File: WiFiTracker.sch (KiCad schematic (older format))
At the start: 33 parts, among them IC1 CP2104, P1 ANT, P2 Battery, P3 USB_B, Q1 MMBT2222A, Q2 MMBT2222A, SW1 SW_RESET, U1 RFM95W-868S2, U2 AP2114, U3 MCP73831T-2ATI/OT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

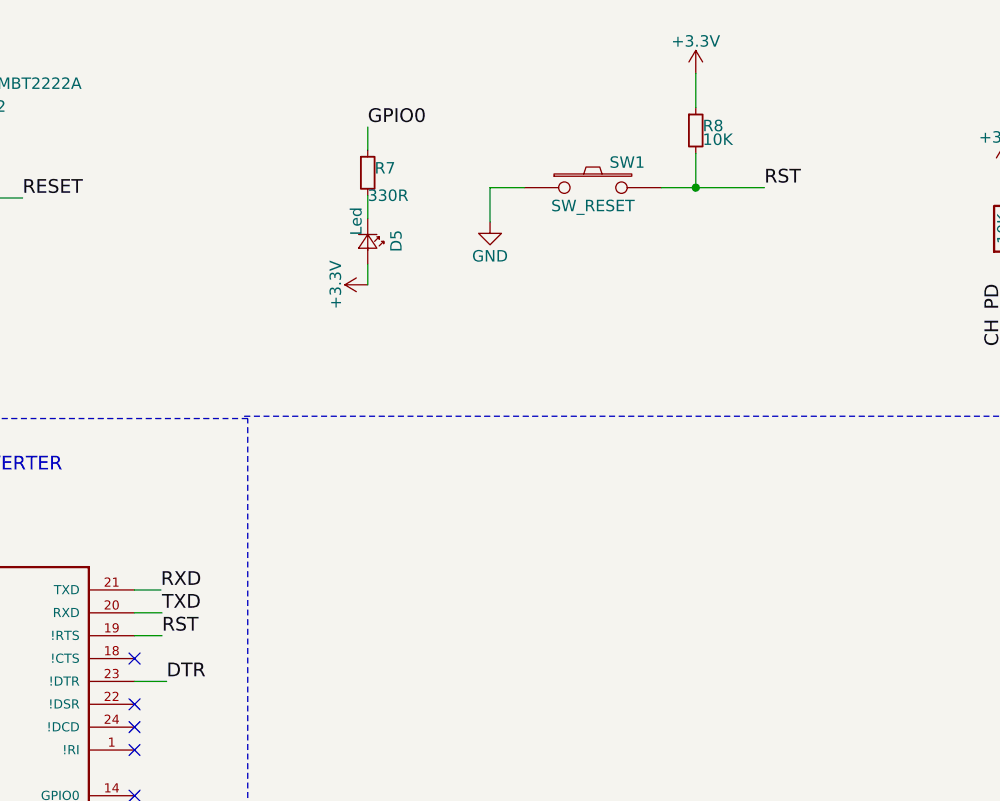
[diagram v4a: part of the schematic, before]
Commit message: Fix Reset connection
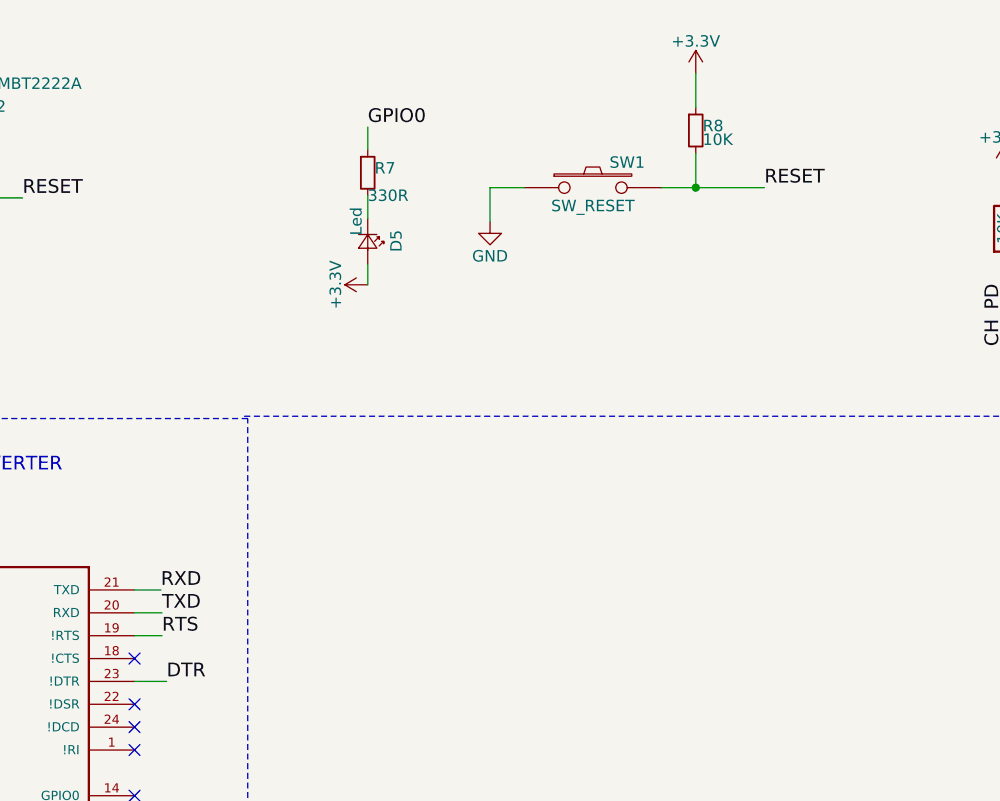
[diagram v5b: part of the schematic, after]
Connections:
- net RESET: now also R8.2, SW1.2
- net RTS: now also IC1.19 (!RTS)
- removed net RST: IC1.19 (!RTS), R8.2, SW1.2
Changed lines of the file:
@@
 Title "LoRaCat: WiFiTracker"
 Date "2017-02-20"
-Rev "0.3"
+Rev "0.4"
 Comp "Electronic Cats"
 Comment1 "Andres Sabas"
@@
 $EndComp
 Text Label 9230 3660 0    60   ~ 0
-RST
+RESET
 Text Notes 1600 600  0    60   ~ 0
 RFM95
@@
 RXD
 Text Label 6595 5620 0    60   ~ 0
-RST
+RTS
 $Comp
 L VCC #PWR022
